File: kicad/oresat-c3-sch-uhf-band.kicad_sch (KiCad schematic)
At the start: 125 parts, among them Q3 NTR4101, Q4 PMV45EN, U16 AX5043, U18 LT5534, U19 BDCN-20-13+, U20 QPC1022, U21 TQP7M9105, U22 LT5534, U25 SN74LVC1G11IDCKRQ1, U26 TLV7041DBV, U27 LP2985AIM5-1.8_NOPB, U29 TQP3M9036, U32 SF2446E, U33 SF2446E, U40 MAX941EUA+, X1 TYKTBLSANF-16.000000

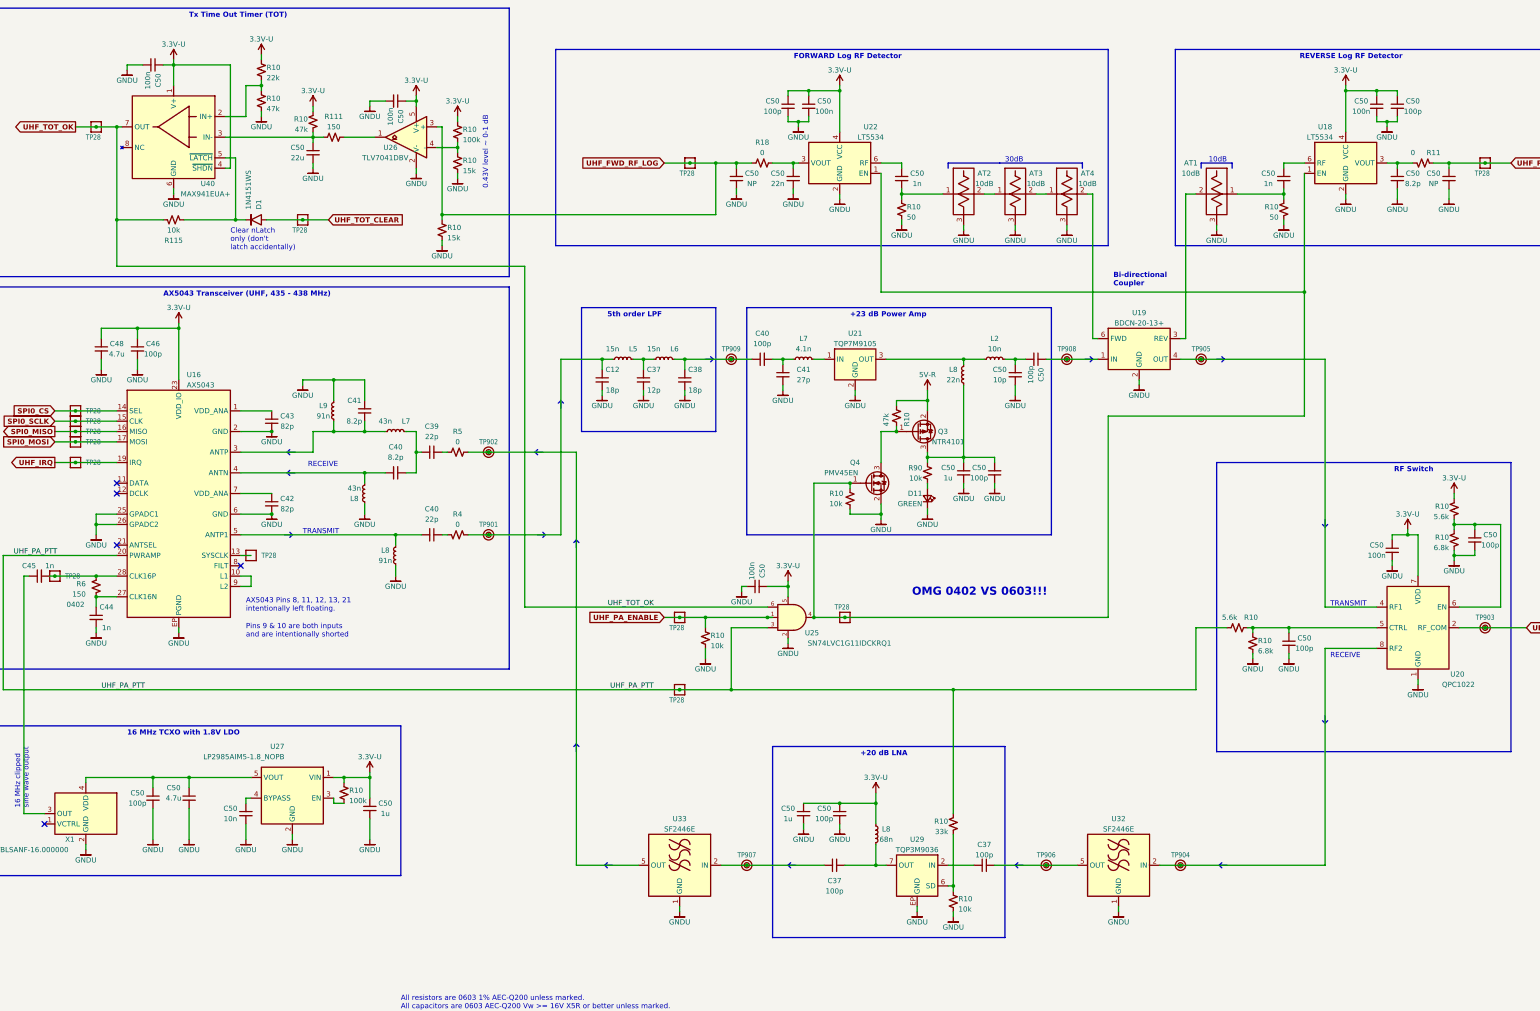
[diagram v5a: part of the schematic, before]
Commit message: Switched all grounds to a single ground, because I can't find a way to overlap ground planes in KiCAD. That's actually not terrible, however, because KiCAD has an anti-plane feature which I used to cut the ground plane between UHF and L radios and L radio and Octavo. So actually I think it came out better than having separate ground planes. Only thing left now are the ~ 40 connections to the Octavo.
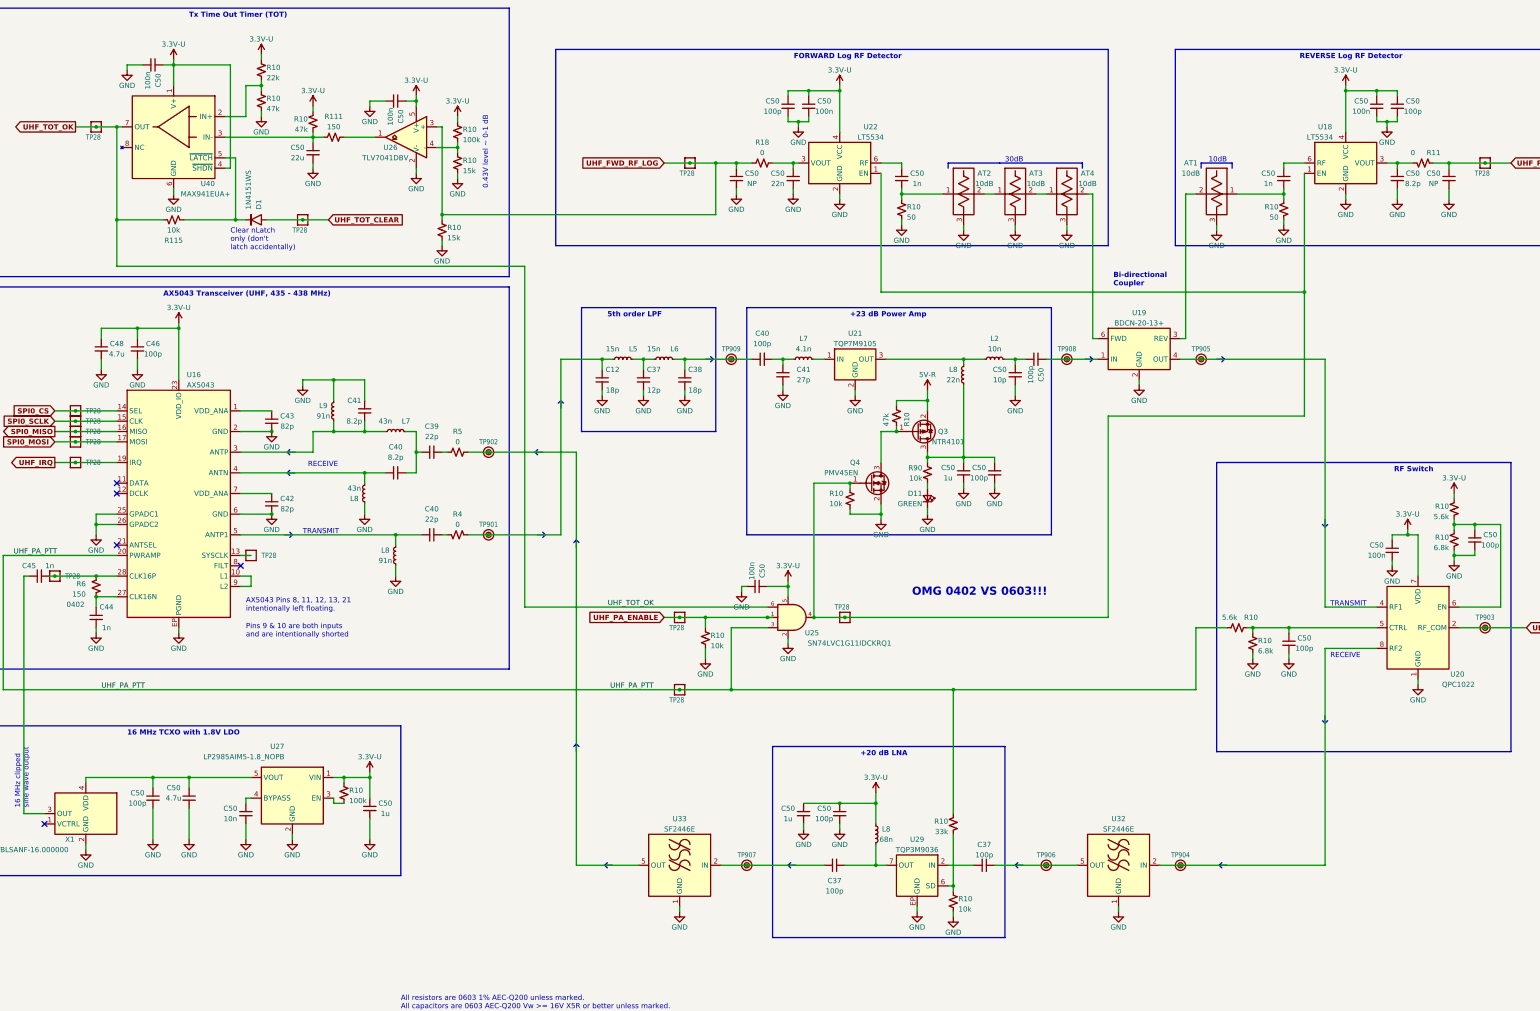
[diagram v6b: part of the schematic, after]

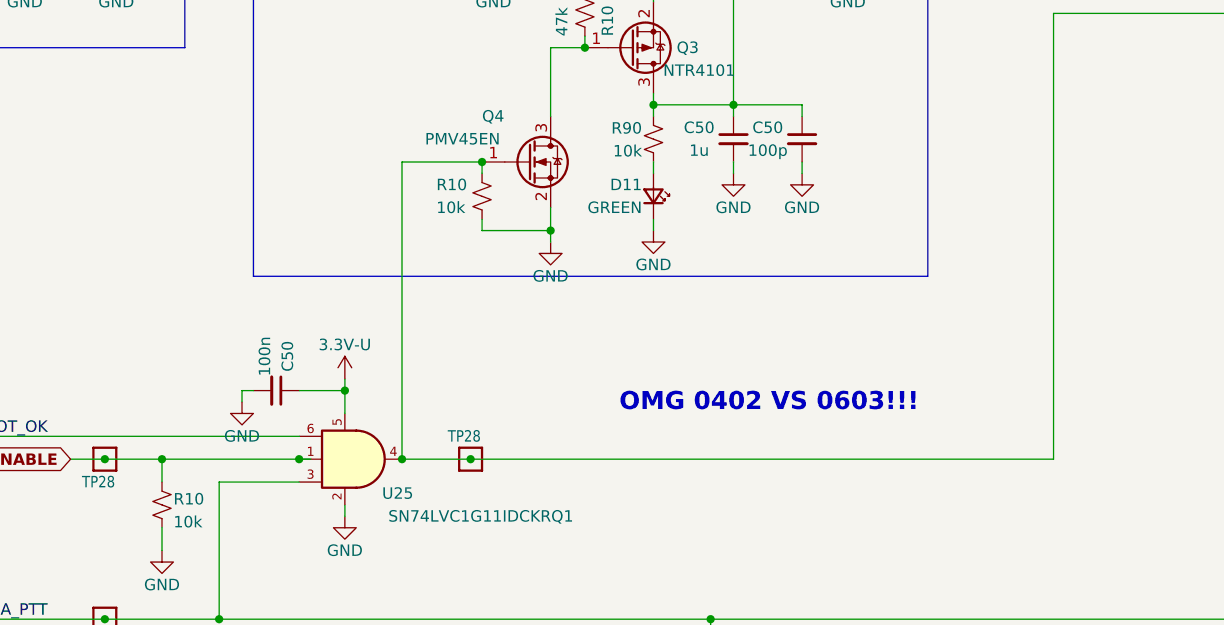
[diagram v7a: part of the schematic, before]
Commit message: An evening of cleanups from the design review. Includes lots of ERC and DRC cleanup, although still over 450 DRC errors mostly from RF keepouts. Fixed PA ground connection, notes on pin reset configuration, and lots of small naggy things. Also cleaned up wierd broken traces on eMMC traces. No longer all same length (sorry Oliver) but it shouldn't affect performance.
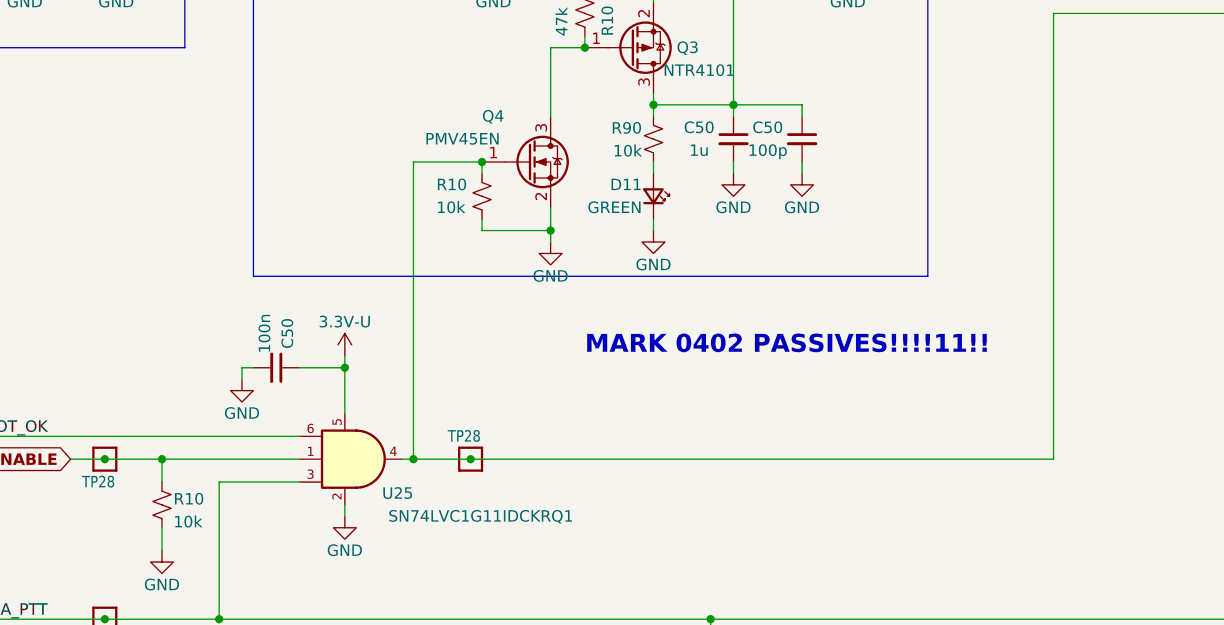
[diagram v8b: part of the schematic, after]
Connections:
- now unconnected: U16.18 (NC), U16.22 (NC), U16.24 (NC), U29.1 (NC), U29.3 (NC), U29.4 (NC), U29.5 (NC), U29.8 (NC)
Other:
- note added: "MARK 0402 PASSIVES!!!!11!!"
- note removed: "OMG 0402 VS 0603!!!"
- moved on the sheet: C50
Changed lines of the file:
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@@
     (rev "6.0")
   )
-  (junction (at 213.36 157.48) (diameter 0) (color 0 0 0 0)
+  (junction (at 213.36 154.94) (diameter 0) (color 0 0 0 0)
   )
   (junction (at 43.18 160.02) (diameter 0) (color 0 0 0 0)
@@
   (junction (at 139.7 144.78) (diameter 0) (color 0 0 0 0)
   )
+  (junction (at 193.04 165.1) (diameter 0) (color 0 0 0 0)
+  )
   (junction (at 63.5 93.98) (diameter 0) (color 0 0 0 0)
   )
@@
   (junction (at 269.24 101.6) (diameter 0) (color 0 0 0 0)
   )
-  (junction (at 193.04 165.1) (diameter 0) (color 0 0 0 0)
-  )
   (junction (at 109.22 119.38) (diameter 0) (color 0 0 0 0)
   )
@@
   (junction (at 384.81 167.64) (diameter 0) (color 0 0 0 0)
   )
+  (junction (at 220.98 165.1) (diameter 0) (color 0 0 0 0)
+  )
   (junction (at 276.86 226.06) (diameter 0) (color 0 0 0 0)
   )
@@
   (junction (at 256.54 101.6) (diameter 0) (color 0 0 0 0)
   )
-  (junction (at 208.28 165.1) (diameter 0) (color 0 0 0 0)
-  )
-  (junction (at 219.71 165.1) (diameter 0) (color 0 0 0 0)
-  )
   (junction (at 336.55 167.64) (diameter 0) (color 0 0 0 0)
   )
@@
     (stroke (width 0) (type default))
   )
-  (wire (pts (xy 201.93 158.75) (xy 201.93 157.48))
+  (wire (pts (xy 201.93 156.21) (xy 201.93 154.94))
     (stroke (width 0) (type default))
   )
@@
     (stroke (width 0) (type default))
   )
-  (wire (pts (xy 213.36 157.48) (xy 208.28 157.48))
+  (wire (pts (xy 213.36 154.94) (xy 208.28 154.94))
     (stroke (width 0) (type default))
   )
@@
     (stroke (width 0) (type default))
   )
+  (wire (pts (xy 220.98 165.1) (xy 227.33 165.1))
+    (stroke (width 0) (type default))
+  )
   (wire (pts (xy 368.3 180.34) (xy 368.3 181.61))
     (stroke (width 0) (type default))
@@
     (stroke (width 0.254) (type default) (color 146 146 146 1))
   )
-  (wire (pts (xy 219.71 132.08) (xy 228.6 132.08))
+  (wire (pts (xy 220.98 132.08) (xy 228.6 132.08))
     (stroke (width 0) (type default))
   )
@@
     (stroke (width 0.254) (type default) (color 146 146 146 1))
   )
+  (wire (pts (xy 193.04 165.1) (xy 208.28 165.1))
+    (stroke (width 0) (type default))
+  )
   (wire (pts (xy 358.14 41.91) (xy 358.14 43.18))
     (stroke (width 0) (type default))
@@
     (stroke (width 0) (type default))
   )
-  (wire (pts (xy 213.36 157.48) (xy 213.36 160.02))
+  (wire (pts (xy 213.36 154.94) (xy 213.36 160.02))
     (stroke (width 0) (type default))
   )
@@
     (stroke (width 0) (type default))
   )
-  (wire (pts (xy 219.71 132.08) (xy 219.71 165.1))
+  (wire (pts (xy 220.98 132.08) (xy 220.98 165.1))
     (stroke (width 0) (type default))
   )
@@
     (stroke (width 0) (type default))
   )
+  (wire (pts (xy 220.98 165.1) (xy 219.71 165.1))
+    (stroke (width 0) (type default))
+  )
   (wire (pts (xy 240.03 111.76) (xy 240.03 113.03))
     (stroke (width 0) (type default))
@@
     (stroke (width 0) (type default))
   )
-  (wire (pts (xy 219.71 165.1) (xy 227.33 165.1))
-    (stroke (width 0) (type default))
-  )
   (wire (pts (xy 96.52 39.37) (xy 96.52 40.64))
     (stroke (width 0) (type default))
@@
     (stroke (width 0) (type default))
   )
-  (wire (pts (xy 201.93 157.48) (xy 203.2 157.48))
+  (wire (pts (xy 201.93 154.94) (xy 203.2 154.94))
     (stroke (width 0) (type default))
   )
@@
     (stroke (width 0) (type default))
   )
-  (wire (pts (xy 209.55 165.1) (xy 208.28 165.1))
-    (stroke (width 0) (type default))
-  )
   (wire (pts (xy 187.96 101.6) (xy 199.39 101.6))
     (stroke (width 0) (type default))
@@
     (stroke (width 0.254) (type default) (color 146 146 146 1))
   )
-  (wire (pts (xy 208.28 165.1) (xy 193.04 165.1))
-    (stroke (width 0) (type default))
-  )
   (wire (pts (xy 388.62 142.24) (xy 382.27 142.24))
     (stroke (width 0) (type default))
@@
     (stroke (width 0) (type default))
   )
-  (wire (pts (xy 213.36 156.21) (xy 213.36 157.48))
+  (wire (pts (xy 213.36 153.67) (xy 213.36 154.94))
     (stroke (width 0) (type default))
   )
@@
     (effects (font (size 1.27 1.27)) (justify left bottom))
   )
+  (text "MARK 0402 PASSIVES!!!!11!!" (at 240.03 153.67 0)
+    (effects (font (size 2 2) (thickness 0.4) bold (color 255 0 0 1)) (justify left bottom))
+  )
   (text "+20 dB LNA" (at 231.14 199.39 0)
     (effects (font (size 1.27 1.27) (thickness 0.254) bold) (justify left bottom))
@@
     (effects (font (size 1.27 1.27) (thickness 0.254) bold) (justify right bottom))
   )
-  (text "OMG 0402 VS 0603!!!\n" (at 243.84 160.02 0)
-    (effects (font (size 2 2) (thickness 0.4) bold (color 255 0 0 1)) (justify left bottom))
-  )
   (text "TRANSMIT" (at 346.71 162.56 0)
     (effects (font (size 1.27 1.27)) (justify left bottom))
@@
     )
   )
-  (symbol (lib_id "power:GND") (at 201.93 158.75 0) (mirror y) (unit 1)
+  (symbol (lib_id "power:GND") (at 201.93 156.21 0) (mirror y) (unit 1)
     (in_bom yes) (on_board yes) (dnp no)
-    (property "Reference" "#PWR0235" (at 201.93 165.1 0)
+    (property "Reference" "#PWR0235" (at 201.93 162.56 0)
       (effects (font (size 1.27 1.27)) hide)
     )
-    (property "Value" "GND" (at 201.93 162.56 0)
+    (property "Value" "GND" (at 201.93 160.02 0)
       (effects (font (size 1.27 1.27)))
     )
-    (property "Footprint" "" (at 201.93 158.75 0)
+    (property "Footprint" "" (at 201.93 156.21 0)
       (effects (font (size 1.27 1.27)) hide)
     )
-    (property "Datasheet" "" (at 201.93 158.75 0)
+    (property "Datasheet" "" (at 201.93 156.21 0)
       (effects (font (size 1.27 1.27)) hide)
     )
@@
     )
   )
-  (symbol (lib_id "oresat-power:3.3V-U") (at 213.36 156.21 0) (mirror y) (unit 1)
+  (symbol (lib_id "oresat-power:3.3V-U") (at 213.36 153.67 0) (mirror y) (unit 1)
     (in_bom yes) (on_board yes) (dnp no) (fields_autoplaced)
-    (property "Reference" "#3V3-U06" (at 213.36 160.02 0)
+    (property "Reference" "#3V3-U06" (at 213.36 157.48 0)
       (effects (font (size 1.27 1.27)) hide)
     )
-    (property "Value" "3.3V-U" (at 213.36 152.4 0)
+    (property "Value" "3.3V-U" (at 213.36 149.86 0)
       (effects (font (size 1.27 1.27)))
     )
-    (property "Footprint" "" (at 213.36 156.21 0)
+    (property "Footprint" "" (at 213.36 153.67 0)
       (effects (font (size 1.27 1.27)) hide)
     )
-    (property "Datasheet" "" (at 213.36 156.21 0)
+    (property "Datasheet" "" (at 213.36 153.67 0)
       (effects (font (size 1.27 1.27)) hide)
     )
@@
     )
   )
-  (symbol (lib_id "Device:C_Small") (at 205.74 157.48 270) (mirror x) (unit 1)
+  (symbol (lib_id "Device:C_Small") (at 205.74 154.94 270) (mirror x) (unit 1)
     (in_bom yes) (on_board yes) (dnp no)
-    (property "Reference" "C50" (at 207.01 153.67 0)
+    (property "Reference" "C50" (at 207.01 151.13 0)
       (effects (font (size 1.27 1.27)))
     )
-    (property "Value" "100n" (at 204.47 153.67 0)
+    (property "Value" "100n" (at 204.47 151.13 0)
       (effects (font (size 1.27 1.27)))
     )
-    (property "Footprint" "Capacitor_SMD:C_0603_1608Metric" (at 205.74 157.48 0)
+    (property "Footprint" "Capacitor_SMD:C_0603_1608Metric" (at 205.74 154.94 0)
       (effects (font (size 1.27 1.27)) hide)
     )
-    (property "Datasheet" "~" (at 205.74 157.48 0)
+    (property "Datasheet" "~" (at 205.74 154.94 0)
       (effects (font (size 1.27 1.27)) hide)
     )
